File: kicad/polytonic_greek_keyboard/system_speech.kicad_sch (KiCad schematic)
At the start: 1 part, among them SW4 SW_SP4T_NR01104

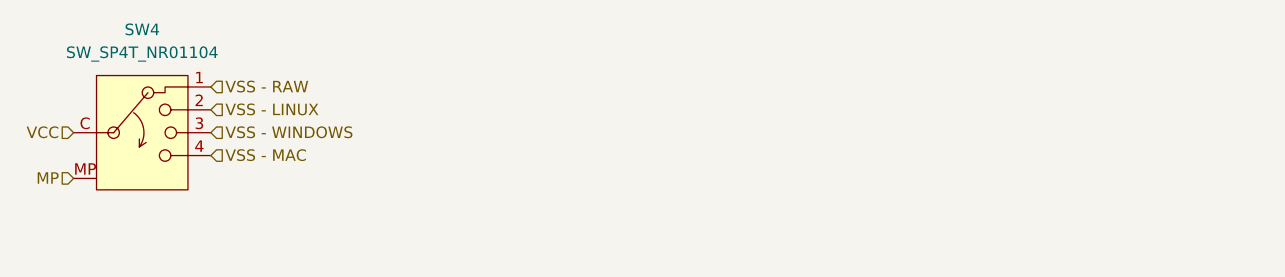
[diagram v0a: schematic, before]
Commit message: [ADD] a more structured approach of the pcb in a way that won't overload the esp32 that is running it
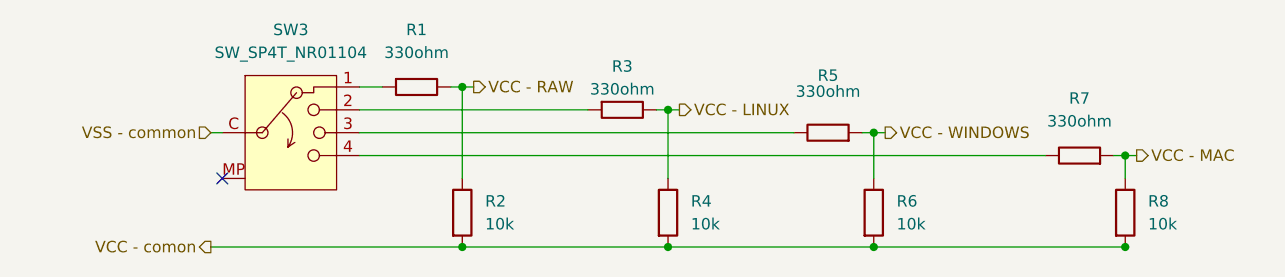
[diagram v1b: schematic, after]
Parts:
- added R1, R3, R5, R7: 330ohm, Resistor_THT:R_Axial_DIN0207_L6.3mm_D2.5mm_P10.16mm_Horizontal, symbol PCM_SL_Resistors:330ohm
- added R2, R4, R6, R8: 10k_0402, Resistor_SMD:R_0402_1005Metric, symbol PCM_4ms_Resistor:10k_0402
- renumbered SW4 to SW3
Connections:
- net MP: no longer names the net of SW3.MP
- net VCC renamed VSS - common
- net VSS - LINUX: no longer names the net of SW3.2
- net VSS - LINUX: now also R3.1
- net VSS - MAC: no longer names the net of SW3.4
- net VSS - MAC: now also R7.2
- net VSS - RAW: no longer names the net of SW3.1
- net VSS - RAW: now also R1.1
- net VSS - WINDOWS: no longer names the net of SW3.3
- net VSS - WINDOWS: now also R5.2
- new net VCC - LINUX: R3.2, R4.1
- new net VCC - MAC: R7.1, R8.1
- new net VCC - RAW: R1.2, R2.1
- new net VCC - WINDOWS: R5.1, R6.1
- new net VCC - comon: R2.2, R4.2, R6.2, R8.2
- no-connect marks 0 -> 1
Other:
- moved on the sheet: SW3

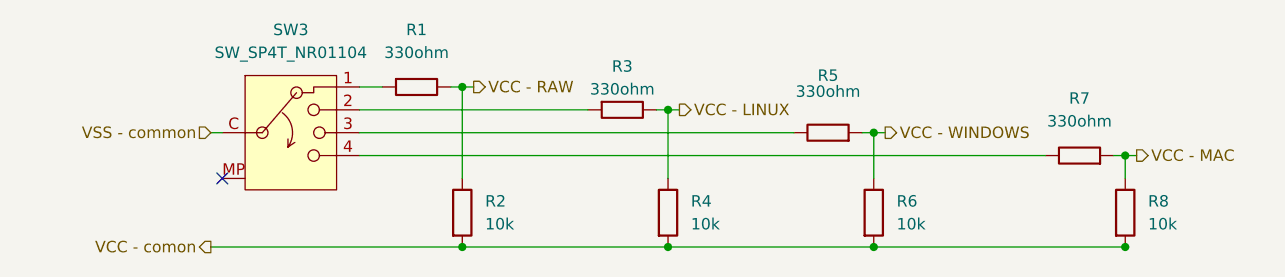
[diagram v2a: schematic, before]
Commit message: [UPDATE] the desing to fit on two separate pcbs
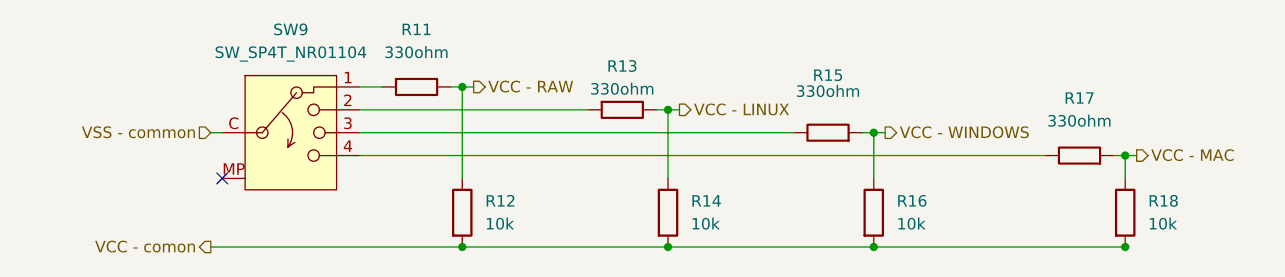
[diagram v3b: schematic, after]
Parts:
- renumbered R1 to R11, R2 to R12, R3 to R13, R4 to R14, R5 to R15, R6 to R16, R7 to R17, R8 to R18, SW3 to SW9
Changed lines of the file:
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@@
 		(on_board yes)
 		(dnp no)
-		(property "Reference" "R5"
+		(property "Reference" "R15"
 			(at 104.14 20.32 0)
 			(effects
@@
 		)
 		(instances
-			(project ""
-				(path "/cbe25a1b-6c02-43c2-9ff9-ba274c7cf6a2/93b6a0fb-c84f-4e1a-be68-67f86d3a12c5"
-					(reference "R5")
+			(project "polytonic_greek_keyboard"
+				(path "/cbe25a1b-6c02-43c2-9ff9-ba274c7cf6a2/8498b325-11fd-4b20-a704-75ec3d8987ef/fb6e2354-ecf3-4898-bccb-a017b889063a"
+					(reference "R15")
 					(unit 1)
 				)
@@
 		(dnp no)
 		(fields_autoplaced yes)
-		(property "Reference" "R4"
+		(property "Reference" "R14"
 			(at 88.9 34.2899 0)
 			(effects
@@
 		)
 		(instances
-			(project ""
-				(path "/cbe25a1b-6c02-43c2-9ff9-ba274c7cf6a2/93b6a0fb-c84f-4e1a-be68-67f86d3a12c5"
-					(reference "R4")
+			(project "polytonic_greek_keyboard"
+				(path "/cbe25a1b-6c02-43c2-9ff9-ba274c7cf6a2/8498b325-11fd-4b20-a704-75ec3d8987ef/fb6e2354-ecf3-4898-bccb-a017b889063a"
+					(reference "R14")
 					(unit 1)
 				)
@@
 		(dnp no)
 		(fields_autoplaced yes)
-		(property "Reference" "R2"
+		(property "Reference" "R12"
 			(at 66.04 34.2899 0)
 			(effects
@@
 		)
 		(instances
-			(project ""
-				(path "/cbe25a1b-6c02-43c2-9ff9-ba274c7cf6a2/93b6a0fb-c84f-4e1a-be68-67f86d3a12c5"
-					(reference "R2")
+			(project "polytonic_greek_keyboard"
+				(path "/cbe25a1b-6c02-43c2-9ff9-ba274c7cf6a2/8498b325-11fd-4b20-a704-75ec3d8987ef/fb6e2354-ecf3-4898-bccb-a017b889063a"
+					(reference "R12")
 					(unit 1)
 				)
@@
 		(dnp no)
 		(fields_autoplaced yes)
-		(property "Reference" "R7"
+		(property "Reference" "R17"
 			(at 132.08 22.86 0)
 			(effects
@@
 		)
 		(instances
-			(project ""
-				(path "/cbe25a1b-6c02-43c2-9ff9-ba274c7cf6a2/93b6a0fb-c84f-4e1a-be68-67f86d3a12c5"
-					(reference "R7")
+			(project "polytonic_greek_keyboard"
+				(path "/cbe25a1b-6c02-43c2-9ff9-ba274c7cf6a2/8498b325-11fd-4b20-a704-75ec3d8987ef/fb6e2354-ecf3-4898-bccb-a017b889063a"
+					(reference "R17")
 					(unit 1)
 				)
@@
 		(dnp no)
 		(fields_autoplaced yes)
-		(property "Reference" "SW3"
+		(property "Reference" "SW9"
 			(at 44.45 15.24 0)
 			(effects
@@
 		)
 		(instances
-			(project ""
-				(path "/cbe25a1b-6c02-43c2-9ff9-ba274c7cf6a2/93b6a0fb-c84f-4e1a-be68-67f86d3a12c5"
-					(reference "SW3")
+			(project "polytonic_greek_keyboard"
+				(path "/cbe25a1b-6c02-43c2-9ff9-ba274c7cf6a2/8498b325-11fd-4b20-a704-75ec3d8987ef/fb6e2354-ecf3-4898-bccb-a017b889063a"
+					(reference "SW9")
 					(unit 1)
 				)
@@
 		(dnp no)
 		(fields_autoplaced yes)
-		(property "Reference" "R8"
+		(property "Reference" "R18"
 			(at 139.7 34.2899 0)
 			(effects
@@
 		)
 		(instances
-			(project ""
-				(path "/cbe25a1b-6c02-43c2-9ff9-ba274c7cf6a2/93b6a0fb-c84f-4e1a-be68-67f86d3a12c5"
-					(reference "R8")
+			(project "polytonic_greek_keyboard"
+				(path "/cbe25a1b-6c02-43c2-9ff9-ba274c7cf6a2/8498b325-11fd-4b20-a704-75ec3d8987ef/fb6e2354-ecf3-4898-bccb-a017b889063a"
+					(reference "R18")
 					(unit 1)
 				)
@@
 		(on_board yes)
 		(dnp no)
-		(property "Reference" "R3"
+		(property "Reference" "R13"
 			(at 81.28 19.304 0)
 			(effects
@@
 		)
 		(instances
-			(project ""
-				(path "/cbe25a1b-6c02-43c2-9ff9-ba274c7cf6a2/93b6a0fb-c84f-4e1a-be68-67f86d3a12c5"
-					(reference "R3")
+			(project "polytonic_greek_keyboard"
+				(path "/cbe25a1b-6c02-43c2-9ff9-ba274c7cf6a2/8498b325-11fd-4b20-a704-75ec3d8987ef/fb6e2354-ecf3-4898-bccb-a017b889063a"
+					(reference "R13")
 					(unit 1)
 				)
@@
 		(dnp no)
 		(fields_autoplaced yes)
-		(property "Reference" "R1"
+		(property "Reference" "R11"
 			(at 58.42 15.24 0)
 			(effects
@@
 		)
 		(instances
-			(project ""
-				(path "/cbe25a1b-6c02-43c2-9ff9-ba274c7cf6a2/93b6a0fb-c84f-4e1a-be68-67f86d3a12c5"
-					(reference "R1")
+			(project "polytonic_greek_keyboard"
+				(path "/cbe25a1b-6c02-43c2-9ff9-ba274c7cf6a2/8498b325-11fd-4b20-a704-75ec3d8987ef/fb6e2354-ecf3-4898-bccb-a017b889063a"
+					(reference "R11")
 					(unit 1)
 				)
@@
 		(dnp no)
 		(fields_autoplaced yes)
-		(property "Reference" "R6"
+		(property "Reference" "R16"
 			(at 111.76 34.2899 0)
 			(effects
@@
 		)
 		(instances
-			(project ""
-				(path "/cbe25a1b-6c02-43c2-9ff9-ba274c7cf6a2/93b6a0fb-c84f-4e1a-be68-67f86d3a12c5"
-					(reference "R6")
+			(project "polytonic_greek_keyboard"
+				(path "/cbe25a1b-6c02-43c2-9ff9-ba274c7cf6a2/8498b325-11fd-4b20-a704-75ec3d8987ef/fb6e2354-ecf3-4898-bccb-a017b889063a"
+					(reference "R16")
 					(unit 1)
 				)

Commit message: [UPDATE] anotation issues
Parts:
- renumbered R11 to R18, R12 to R19, R13 to R20, R14 to R21, R15 to R22, R16 to R23, R17 to R24, R18 to R25, SW9 to SW5
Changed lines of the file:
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@@
 		(on_board yes)
 		(dnp no)
-		(property "Reference" "R15"
+		(property "Reference" "R22"
 			(at 104.14 20.32 0)
 			(effects
@@
 			(project "polytonic_greek_keyboard"
 				(path "/cbe25a1b-6c02-43c2-9ff9-ba274c7cf6a2/8498b325-11fd-4b20-a704-75ec3d8987ef/fb6e2354-ecf3-4898-bccb-a017b889063a"
-					(reference "R15")
+					(reference "R22")
 					(unit 1)
 				)
@@
 		(dnp no)
 		(fields_autoplaced yes)
-		(property "Reference" "R14"
+		(property "Reference" "R21"
 			(at 88.9 34.2899 0)
 			(effects
@@
 			(project "polytonic_greek_keyboard"
 				(path "/cbe25a1b-6c02-43c2-9ff9-ba274c7cf6a2/8498b325-11fd-4b20-a704-75ec3d8987ef/fb6e2354-ecf3-4898-bccb-a017b889063a"
-					(reference "R14")
+					(reference "R21")
 					(unit 1)
 				)
@@
 		(dnp no)
 		(fields_autoplaced yes)
-		(property "Reference" "R12"
+		(property "Reference" "R19"
 			(at 66.04 34.2899 0)
 			(effects
@@
 			(project "polytonic_greek_keyboard"
 				(path "/cbe25a1b-6c02-43c2-9ff9-ba274c7cf6a2/8498b325-11fd-4b20-a704-75ec3d8987ef/fb6e2354-ecf3-4898-bccb-a017b889063a"
-					(reference "R12")
+					(reference "R19")
 					(unit 1)
 				)
@@
 		(dnp no)
 		(fields_autoplaced yes)
-		(property "Reference" "R17"
+		(property "Reference" "R24"
 			(at 132.08 22.86 0)
 			(effects
@@
 			(project "polytonic_greek_keyboard"
 				(path "/cbe25a1b-6c02-43c2-9ff9-ba274c7cf6a2/8498b325-11fd-4b20-a704-75ec3d8987ef/fb6e2354-ecf3-4898-bccb-a017b889063a"
-					(reference "R17")
+					(reference "R24")
 					(unit 1)
 				)
@@
 		(dnp no)
 		(fields_autoplaced yes)
-		(property "Reference" "SW9"
+		(property "Reference" "SW5"
 			(at 44.45 15.24 0)
 			(effects
@@
 			(project "polytonic_greek_keyboard"
 				(path "/cbe25a1b-6c02-43c2-9ff9-ba274c7cf6a2/8498b325-11fd-4b20-a704-75ec3d8987ef/fb6e2354-ecf3-4898-bccb-a017b889063a"
-					(reference "SW9")
+					(reference "SW5")
 					(unit 1)
 				)
@@
 		(dnp no)
 		(fields_autoplaced yes)
-		(property "Reference" "R18"
+		(property "Reference" "R25"
 			(at 139.7 34.2899 0)
 			(effects
@@
 			(project "polytonic_greek_keyboard"
 				(path "/cbe25a1b-6c02-43c2-9ff9-ba274c7cf6a2/8498b325-11fd-4b20-a704-75ec3d8987ef/fb6e2354-ecf3-4898-bccb-a017b889063a"
-					(reference "R18")
+					(reference "R25")
 					(unit 1)
 				)
@@
 		(on_board yes)
 		(dnp no)
-		(property "Reference" "R13"
+		(property "Reference" "R20"
 			(at 81.28 19.304 0)
 			(effects
@@
 			(project "polytonic_greek_keyboard"
 				(path "/cbe25a1b-6c02-43c2-9ff9-ba274c7cf6a2/8498b325-11fd-4b20-a704-75ec3d8987ef/fb6e2354-ecf3-4898-bccb-a017b889063a"
-					(reference "R13")
+					(reference "R20")
 					(unit 1)
 				)
@@
 		(dnp no)
 		(fields_autoplaced yes)
-		(property "Reference" "R11"
+		(property "Reference" "R18"
 			(at 58.42 15.24 0)
 			(effects
@@
 			(project "polytonic_greek_keyboard"
 				(path "/cbe25a1b-6c02-43c2-9ff9-ba274c7cf6a2/8498b325-11fd-4b20-a704-75ec3d8987ef/fb6e2354-ecf3-4898-bccb-a017b889063a"
-					(reference "R11")
+					(reference "R18")
 					(unit 1)
 				)
@@
 		(dnp no)
 		(fields_autoplaced yes)
-		(property "Reference" "R16"
+		(property "Reference" "R23"
 			(at 111.76 34.2899 0)
 			(effects
@@
 			(project "polytonic_greek_keyboard"
 				(path "/cbe25a1b-6c02-43c2-9ff9-ba274c7cf6a2/8498b325-11fd-4b20-a704-75ec3d8987ef/fb6e2354-ecf3-4898-bccb-a017b889063a"
-					(reference "R16")
+					(reference "R23")
 					(unit 1)
 				)

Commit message: [UPDATE] the final merged version of the schematic before splitting into two separate kicad projects
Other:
- company: (none) -> Henry's Software House
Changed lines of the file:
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@@
 	(generator_version "9.0")
 	(paper "A4")
+	(title_block
+		(rev "1 - do not edit connector pin layout.")
+		(company "Henry's Software House")
+	)
 	(junction
 		(at 63.5 21.59)
